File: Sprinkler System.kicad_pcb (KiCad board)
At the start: 2 copper layers, 165 x 85 mm, 80 parts, among them J1 Main Supply, J2 XFMR_Out, J20 Station_0, J21 Station_1, J22 Station_2, J23 Station_3, J24 Station_4, J25 Station_5, J3 XFMR_In, J4 Conn_Button, J5 UART0, J6 I2C, K1 G3MB-202P, K20 G5LE-1-DC5, K21 G5LE-1-DC5, K22 G5LE-1-DC5, K23 G5LE-1-DC5, K24 G5LE-1-DC5, K25 G5LE-1-DC5, SW1 EN, SW2 BOOT, U1 AMS1117-3.3, U2 EL817, U3 HLK-PM01, U4 ESP32-WROOM-32U, U5 ULN2803A

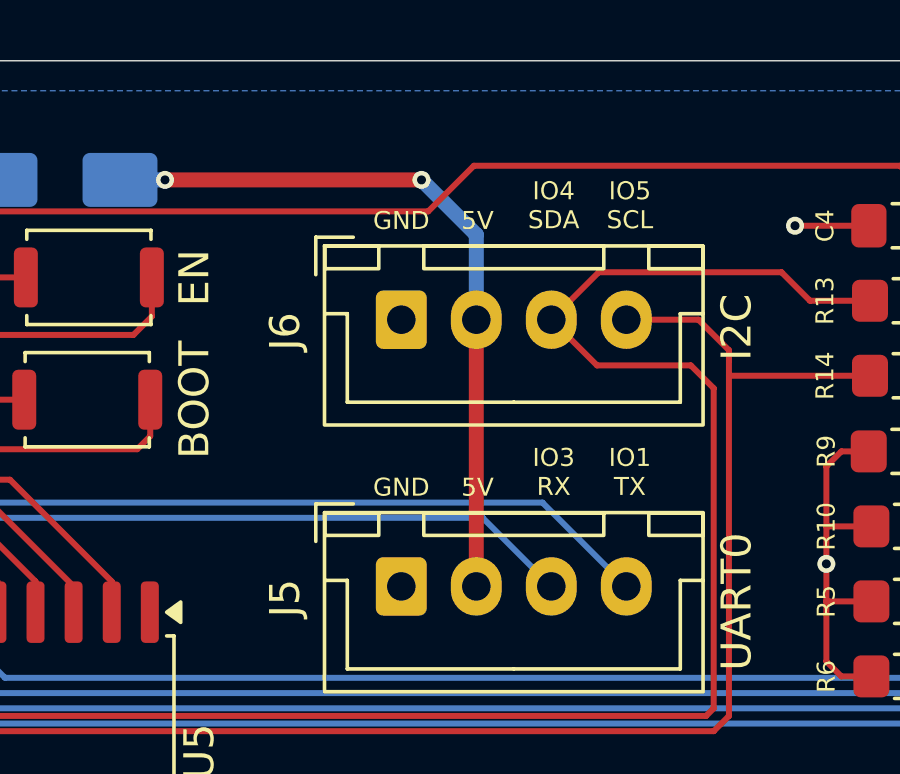
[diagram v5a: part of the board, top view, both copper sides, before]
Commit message: Add JP1 solder jumper to select J6 I2C-header supply (3V3 default)
The I2C expansion header J6 previously took the raw +5V_UART branch on
pin 2, which would put 5V on the SDA/SCL pull-ups and any 3V3-logic
peripheral. JP1 (3-way solder jumper on the back) selects J6's VCC:
default-bridged 1-2 = +3V3, re-bridge 2-3 = +5V. J6 pin 2 is now the
/J6_VCC net; J5 pin 2 keeps the true +5V_UART (re-fed from the rail on
F.Cu past the IO-routing on the back), so UART-adapter powering and the
D2 back-feed block are unaffected.

Scope note: the optional TCA9406 level-shifter and SDA/SCL bypass
jumpers from the original plan were dropped - the J5/J6 corner is too
congested to route them cleanly on this revision, and the supply
jumper alone covers the intended use (run a 3V3 I2C device safely, or
switch to 5V if ever needed). Can be revisited interactively later.

Jumper is on B.Cu, silk-labelled. ERC/DRC: 0 violations; zones refilled.

Co-Authored-By: Claude Fable 5 <noreply@anthropic.com>
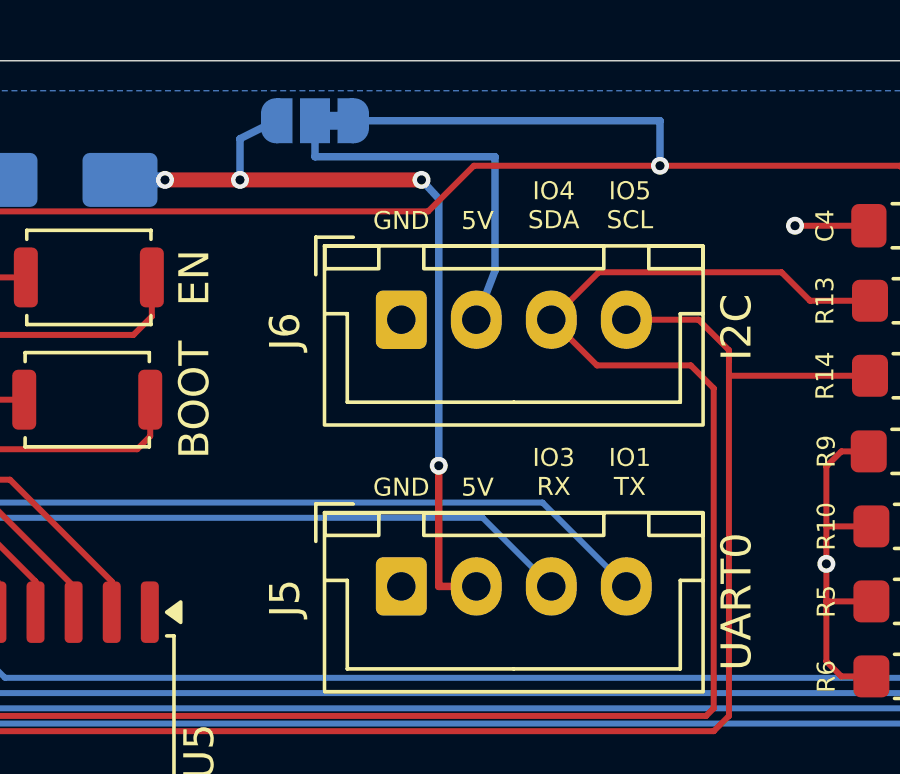
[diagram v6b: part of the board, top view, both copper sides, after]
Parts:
- added JP1: I2C_VCC, SolderJumper-3_P1.3mm_Bridged12_RoundedPad1.0x1.5mm_NumberLabels, B.Cu at (178.5, 48.0)
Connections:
- J6 pad 2: /+5V_UART -> /J6_VCC
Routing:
- net /J6_VCC: track 0.00 -> 12.7 mm
- net +3V3: track 178.9 -> 190.6 mm, vias 2 -> 3
- net /+5V_UART: track 24.4 -> 27.8 mm, vias 2 -> 4
